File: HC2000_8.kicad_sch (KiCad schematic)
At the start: 24 parts

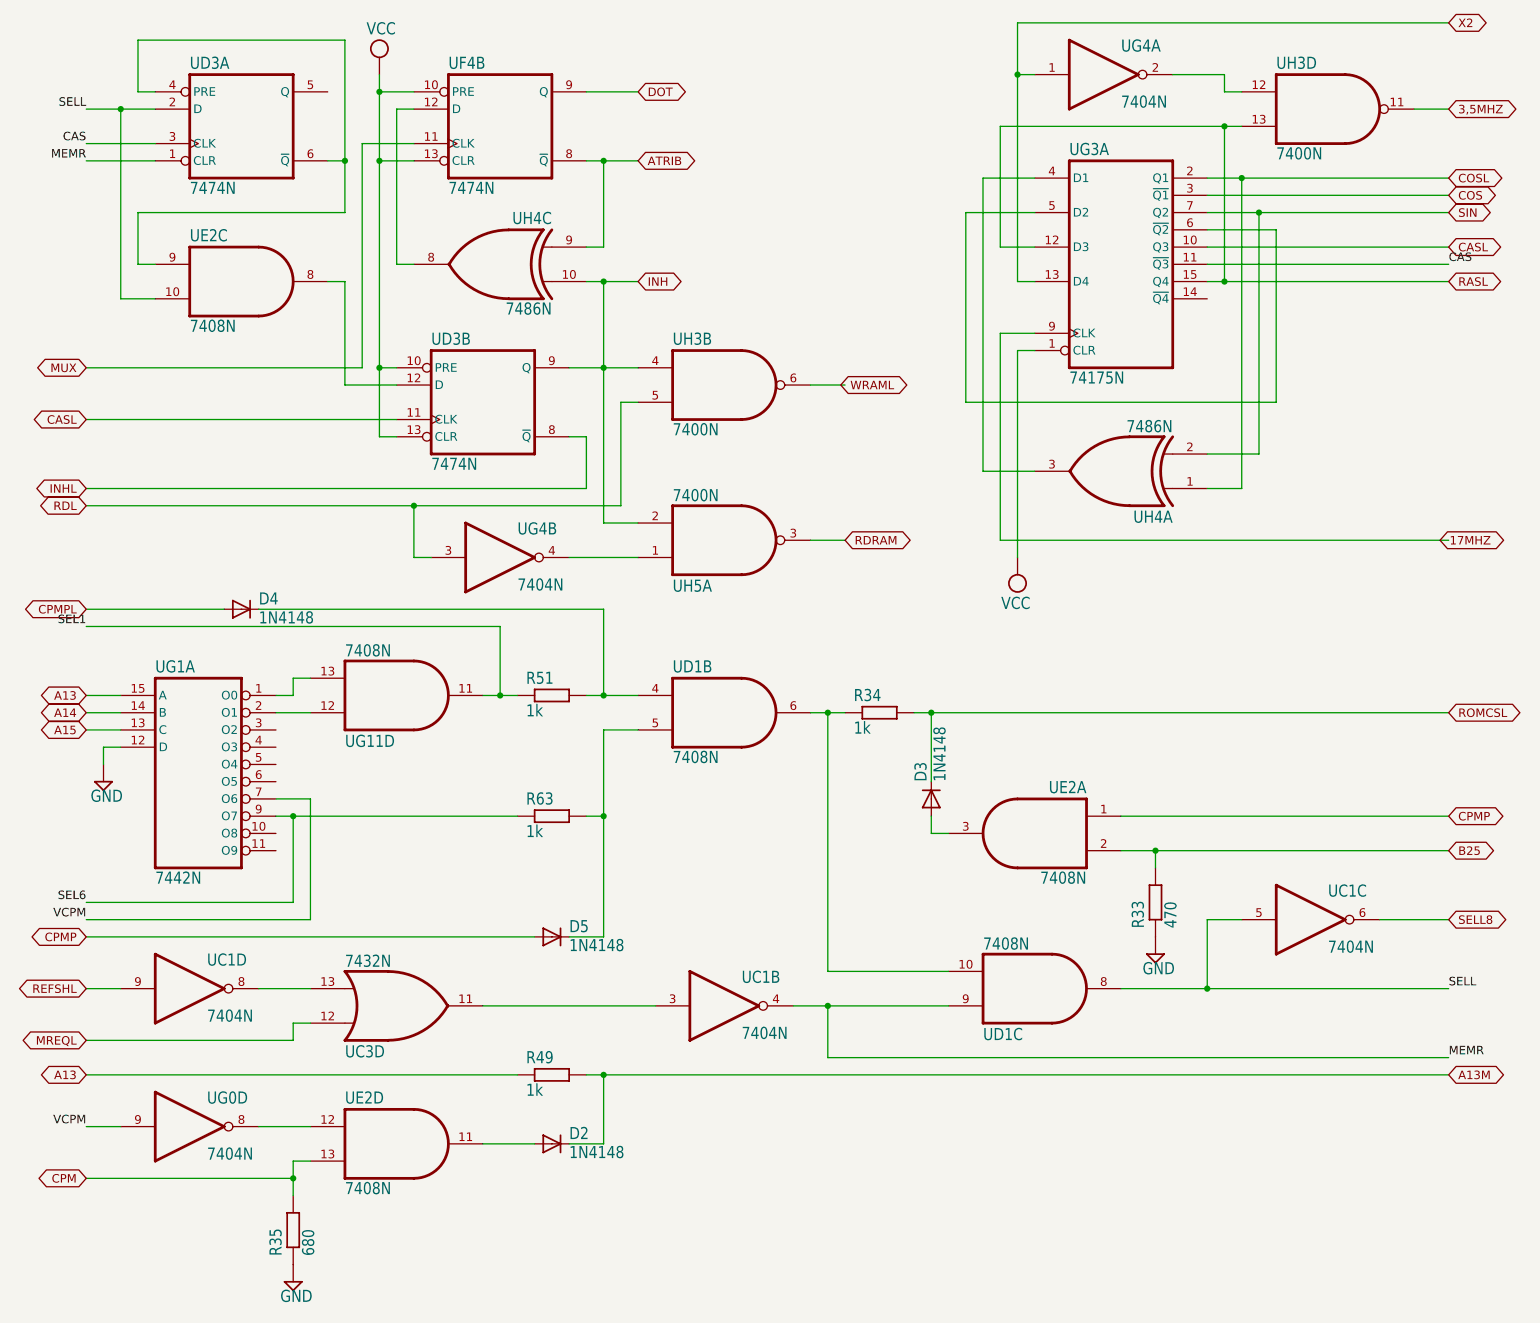
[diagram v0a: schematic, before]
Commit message: Fix errors (IC & unnoticed cut for 1 EPROM)
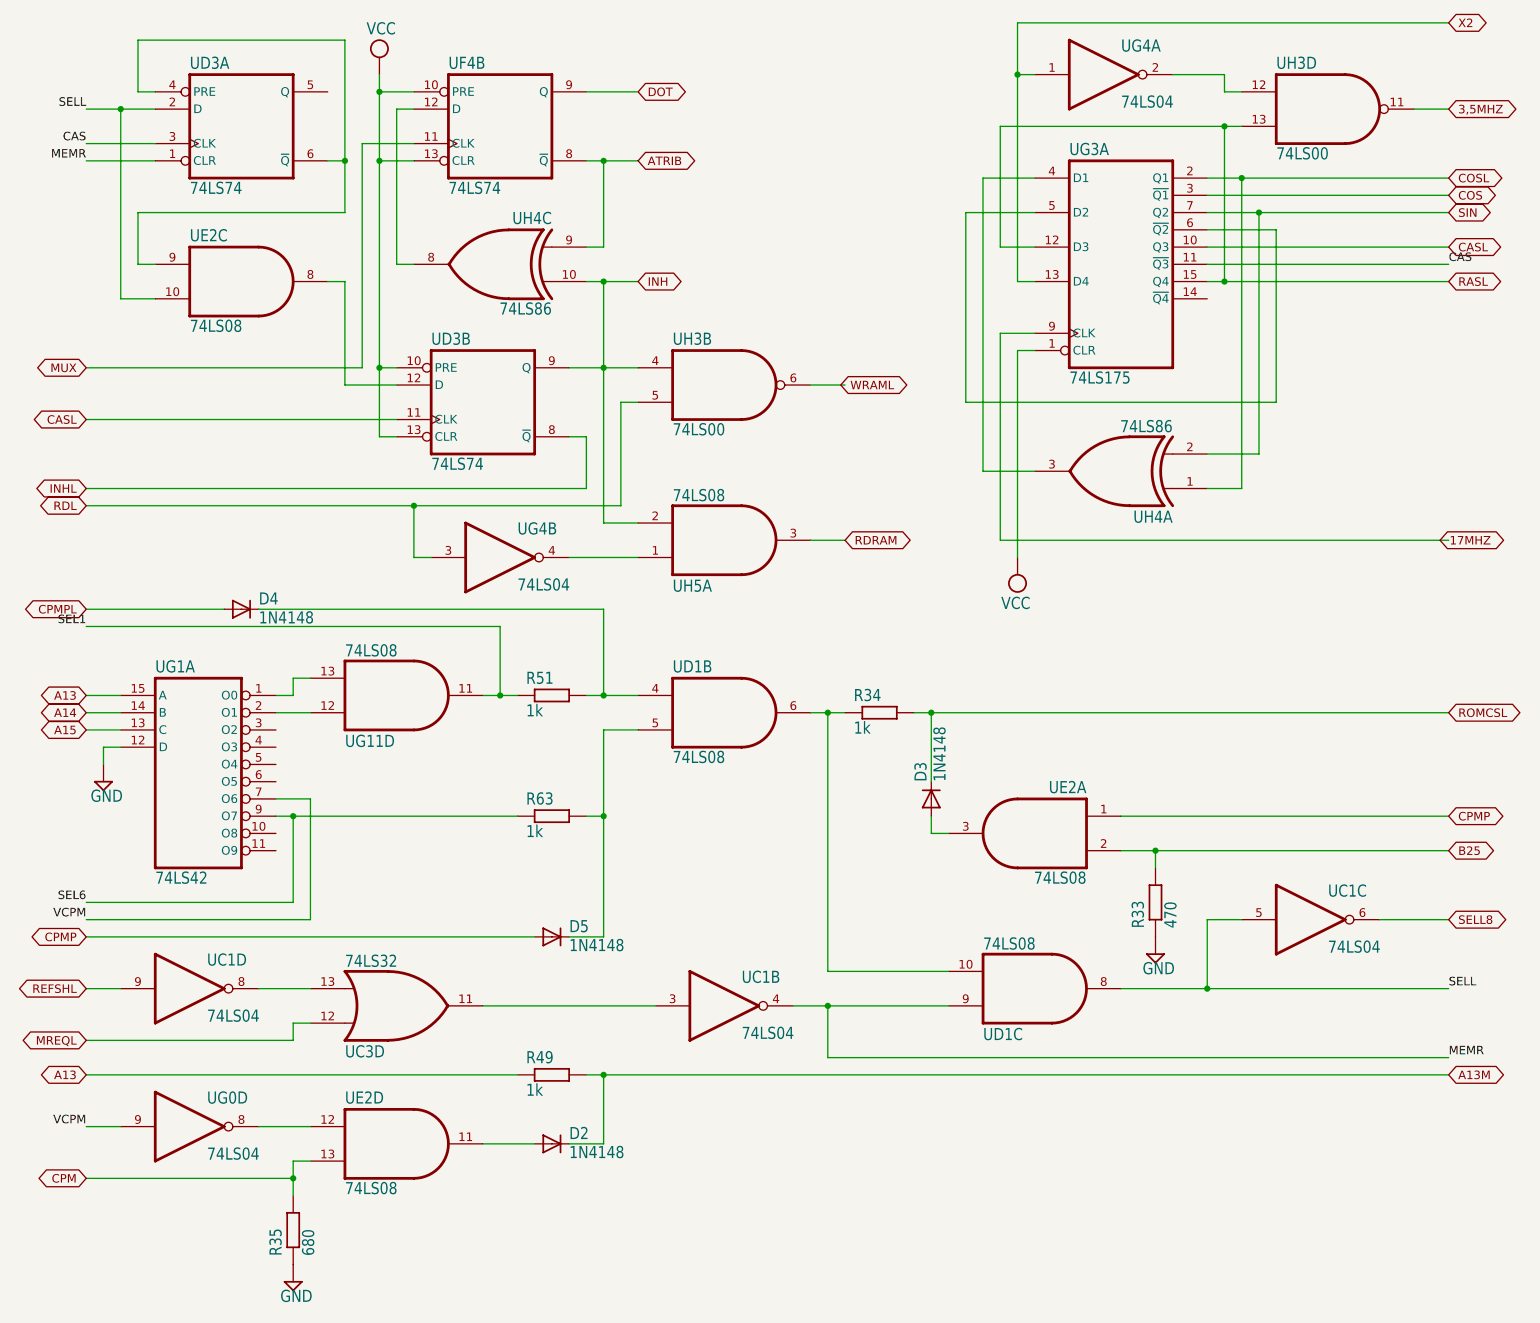
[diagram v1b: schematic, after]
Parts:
- UC1, UG0, UG4: value 7404N -> 74LS04
- UC3: value 7432N -> 74LS32
- UD1, UE2, UG11: value 7408N -> 74LS08
- UD3, UF4: value 7474N -> 74LS74
- UG1: value 7442N -> 74LS42
- UG3: value 74175N -> 74LS175
- UH3: value 7400N -> 74LS00
- UH4: value 7486N -> 74LS86
- UH5: value 7400N -> 74LS08; symbol HC2000:7400N -> HC2000:7408N
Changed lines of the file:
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@@
       (effects (font (size 1.778 1.5113)) (justify left bottom))
     )
-    (property "Value" "7404N" (at 139.7 167.64 0)
+    (property "Value" "74LS04" (at 139.7 167.64 0)
       (effects (font (size 1.778 1.5113)) (justify left bottom))
     )
@@
       (effects (font (size 1.778 1.5113)) (justify left bottom))
     )
-    (property "Value" "7404N" (at 60.96 165.1 0)
+    (property "Value" "74LS04" (at 60.96 165.1 0)
       (effects (font (size 1.778 1.5113)) (justify left bottom))
     )
@@
       (effects (font (size 1.778 1.5113)) (justify left bottom))
     )
-    (property "Value" "7408N" (at 81.28 190.5 0)
+    (property "Value" "74LS08" (at 81.28 190.5 0)
       (effects (font (size 1.778 1.5113)) (justify left bottom))
     )
@@
       (effects (font (size 1.778 1.5113)) (justify left bottom))
     )
-    (property "Value" "7400N" (at 218.44 38.1 0)
+    (property "Value" "74LS00" (at 218.44 38.1 0)
       (effects (font (size 1.778 1.5113)) (justify left bottom))
     )
@@
       (effects (font (size 1.778 1.5113)) (justify left bottom))
     )
-    (property "Value" "7404N" (at 60.96 185.42 0)
+    (property "Value" "74LS04" (at 60.96 185.42 0)
       (effects (font (size 1.778 1.5113)) (justify left bottom))
     )
@@
       (effects (font (size 1.778 1.5113)) (justify left bottom))
     )
-    (property "Value" "7408N" (at 81.28 109.22 0)
+    (property "Value" "74LS08" (at 81.28 109.22 0)
       (effects (font (size 1.778 1.5113)) (justify left bottom))
     )
@@
       (effects (font (size 1.778 1.5113)) (justify left bottom))
     )
-    (property "Value" "7408N" (at 58.42 63.5 0)
+    (property "Value" "74LS08" (at 58.42 63.5 0)
       (effects (font (size 1.778 1.5113)) (justify left bottom))
     )
@@
       (effects (font (size 1.778 1.5113)) (justify left bottom))
     )
-    (property "Value" "7404N" (at 106.68 101.6 0)
+    (property "Value" "74LS04" (at 106.68 101.6 0)
       (effects (font (size 1.778 1.5113)) (justify left bottom))
     )
@@
       (effects (font (size 1.778 1.5113)) (justify left bottom))
     )
-    (property "Value" "7486N" (at 203.2 76.2 0)
+    (property "Value" "74LS86" (at 203.2 76.2 0)
       (effects (font (size 1.778 1.5113)) (justify left bottom))
     )
@@
       (effects (font (size 1.778 1.5113)) (justify left bottom))
     )
-    (property "Value" "7408N" (at 129.54 127 0)
+    (property "Value" "74LS08" (at 129.54 127 0)
       (effects (font (size 1.778 1.5113)) (justify left bottom))
     )
@@
       (effects (font (size 1.778 1.5113)) (justify left bottom))
     )
-    (property "Value" "7474N" (at 58.42 43.18 0)
+    (property "Value" "74LS74" (at 58.42 43.18 0)
       (effects (font (size 1.778 1.5113)) (justify left bottom))
     )
@@
       (effects (font (size 1.778 1.5113)) (justify left bottom))
     )
-    (property "Value" "7400N" (at 129.54 78.74 0)
+    (property "Value" "74LS00" (at 129.54 78.74 0)
       (effects (font (size 1.778 1.5113)) (justify left bottom))
     )
@@
       (effects (font (size 1.778 1.5113)) (justify left bottom))
     )
-    (property "Value" "74175N" (at 187.96 71.12 0)
+    (property "Value" "74LS175" (at 187.96 71.12 0)
       (effects (font (size 1.778 1.5113)) (justify left bottom))
     )
@@
       (effects (font (size 1.778 1.5113)) (justify left bottom))
     )
-    (property "Value" "7474N" (at 93.98 83.82 0)
+    (property "Value" "74LS74" (at 93.98 83.82 0)
       (effects (font (size 1.778 1.5113)) (justify left bottom))
     )
@@
       (effects (font (size 1.778 1.5113)) (justify left bottom))
     )
-    (property "Value" "7408N" (at 175.26 152.4 0)
+    (property "Value" "74LS08" (at 175.26 152.4 0)
       (effects (font (size 1.778 1.5113)) (justify left bottom))
     )
@@
       (effects (font (size 1.778 1.5113)) (justify left bottom))
     )
-    (property "Value" "7432N" (at 81.28 154.94 0)
+    (property "Value" "74LS32" (at 81.28 154.94 0)
       (effects (font (size 1.778 1.5113)) (justify left bottom))
     )
@@
       (effects (font (size 1.778 1.5113)) (justify left bottom))
     )
-    (property "Value" "7442N" (at 53.34 144.78 0)
+    (property "Value" "74LS42" (at 53.34 144.78 0)
       (effects (font (size 1.778 1.5113)) (justify left bottom))
     )
@@
       (effects (font (size 1.778 1.5113)) (justify left bottom))
     )
-    (property "Value" "7404N" (at 195.58 30.48 0)
+    (property "Value" "74LS04" (at 195.58 30.48 0)
       (effects (font (size 1.778 1.5113)) (justify left bottom))
     )
@@
       (effects (font (size 1.778 1.5113)) (justify left bottom))
     )
-    (property "Value" "7486N" (at 111.76 60.96 0)
+    (property "Value" "74LS86" (at 111.76 60.96 0)
       (effects (font (size 1.778 1.5113)) (justify left bottom))
     )
@@
       (effects (font (size 1.778 1.5113)) (justify left bottom))
     )
-    (property "Value" "7404N" (at 226.06 154.94 0)
+    (property "Value" "74LS04" (at 226.06 154.94 0)
       (effects (font (size 1.778 1.5113)) (justify left bottom))
     )
@@
       (effects (font (size 1.778 1.5113)) (justify left bottom))
     )
-    (property "Value" "7408N" (at 190.5 144.78 0)
+    (property "Value" "74LS08" (at 190.5 144.78 0)
       (effects (font (size 1.778 1.5113)) (justify left bottom))
     )
@@
       (effects (font (size 1.778 1.5113)) (justify left bottom))
     )
-    (property "Value" "7474N" (at 96.52 43.18 0)
+    (property "Value" "74LS74" (at 96.52 43.18 0)
       (effects (font (size 1.778 1.5113)) (justify left bottom))
     )
@@
     )
   )
-  (symbol (lib_id "HC2000:7400N") (at 137.16 93.98 0) (mirror x) (unit 1)
+  (symbol (lib_id "HC2000:7408N") (at 137.16 93.98 0) (mirror x) (unit 1)
     (in_bom yes) (on_board yes) (dnp no)
     (property "Reference" "UH5" (at 129.54 99.695 0)
       (effects (font (size 1.778 1.5113)) (justify left bottom))
     )
-    (property "Value" "7400N" (at 129.54 86.36 0)
-      (effects (font (size 1.778 1.5113)) (justify left bottom))
-    )
+    (property "Value" "74LS08" (at 129.54 86.36 0)
+      (effects (font (size 1.778 1.5113)) (justify left bottom))
+    )
